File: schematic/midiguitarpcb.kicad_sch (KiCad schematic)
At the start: 35 parts, among them J1 USB_C_Receptacle_USB2.0_16P, J2 AudioJack3_Switch, SW1 SW_Omron_B3FS, U1 AMS1117-3.3, U2 DIN-504D-M5, U3 STM32H743ZITx

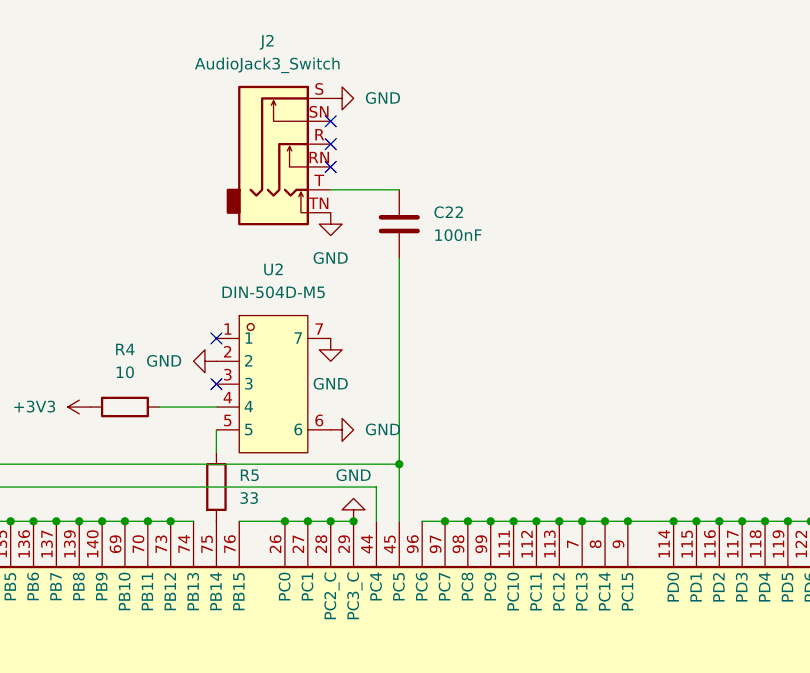
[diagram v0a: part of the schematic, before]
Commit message: chore(wip): about to remove usb code
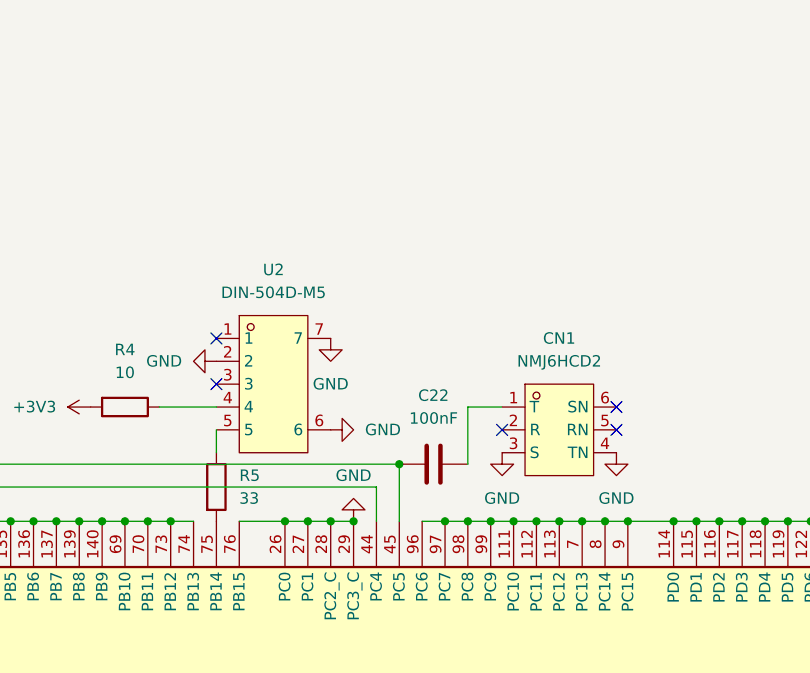
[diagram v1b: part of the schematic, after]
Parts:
- removed J2: AudioJack3_Switch, Connector_Audio:Jack_6.35mm_Neutrik_NMJ6HCD2_Horizontal, symbol Connector_Audio:AudioJack3_Switch
- added CN1: NMJ6HCD2, audio:AUDIO-TH_NMJ6HCD2, symbol audio:NMJ6HCD2
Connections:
- net GND: now also CN1.3 (S), CN1.4 (TN)
- net at C22.1: now also U3.40 (PA4), U3.45 (PC5)
- new net: C22.2, CN1.1 (T)
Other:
- moved on the sheet: C22

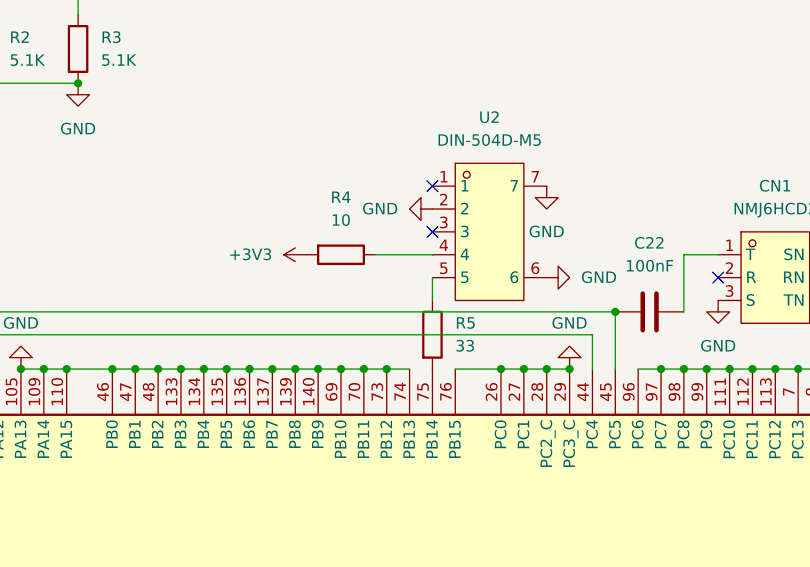
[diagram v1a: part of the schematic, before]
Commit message: fix(pcb): midi resistors swapped
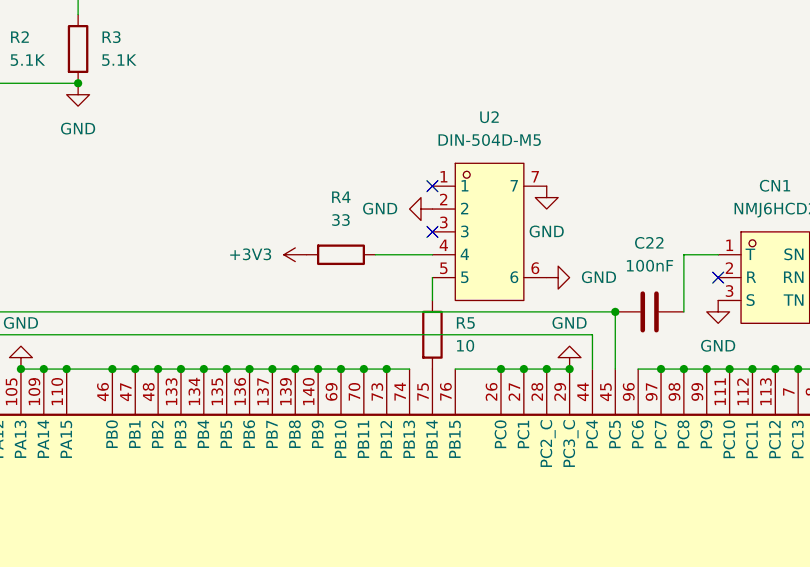
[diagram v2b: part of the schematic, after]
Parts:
- R4: value 10 -> 33
- R5: value 33 -> 10
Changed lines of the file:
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@@
 			)
 		)
-		(property "Value" "10"
+		(property "Value" "33"
 			(at 163.83 71.12 90)
 			(effects
@@
 			)
 		)
-		(property "Value" "33"
+		(property "Value" "10"
 			(at 176.53 85.0899 0)
 			(effects

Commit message: feat(schematic): redo with 2nd opamp
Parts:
- added R5, R6: 100K, Resistor_SMD:R_0402_1005Metric, symbol Device:R
- renumbered C18 to C12, C19 to C17, C20 to C18, C21 to C19, C8 to C20, C17 to C21, C12 to C8, R5 to R7
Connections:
- net +3V3: no longer C20.1, C21.1, U3.32 (VREF+)
- net GND: now also R6.2; no longer U3.1 (PE2), U3.10 (PF0), U3.100 (PA8), U3.101 (PA9), U3.102 (PA10), U3.105 (PA13), U3.109 (PA14), U3.11 (PF1), U3.110 (PA15), U3.111 (PC10), U3.112 (PC11), U3.113 (PC12), U3.114 (PD0), U3.115 (PD1), U3.116 (PD2), U3.117 (PD3), U3.118 (PD4), U3.119 (PD5), U3.12 (PF2), U3.122 (PD6), U3.123 (PD7), U3.124 (PG9), U3.125 (PG10), U3.126 (PG11), U3.127 (PG12), U3.128 (PG13), U3.129 (PG14), U3.13 (PF3), U3.132 (PG15), U3.133 (PB3), U3.134 (PB4), U3.135 (PB5), U3.136 (PB6), U3.137 (PB7), U3.139 (PB8), U3.14 (PF4), U3.140 (PB9), U3.141 (PE0), U3.142 (PE1), U3.15 (PF5), U3.18 (PF6), U3.19 (PF7), U3.2 (PE3), U3.20 (PF8), U3.21 (PF9), U3.22 (PF10), U3.23 (PH0), U3.24 (PH1), U3.26 (PC0), U3.27 (PC1), U3.28 (PC2_C), U3.29 (PC3_C), U3.3 (PE4), U3.34 (PA0), U3.35 (PA1), U3.36 (PA2), U3.37 (PA3), U3.4 (PE5), U3.41 (PA5), U3.42 (PA6), U3.46 (PB0), U3.47 (PB1), U3.48 (PB2), U3.49 (PF11), U3.5 (PE6), U3.50 (PF12), U3.53 (PF13), U3.54 (PF14), U3.55 (PF15), U3.56 (PG0), U3.57 (PG1), U3.58 (PE7), U3.59 (PE8), U3.60 (PE9), U3.63 (PE10), U3.64 (PE11), U3.65 (PE12), U3.66 (PE13), U3.67 (PE14), U3.68 (PE15), U3.69 (PB10), U3.7 (PC13), U3.70 (PB11), U3.73 (PB12), U3.74 (PB13), U3.76 (PB15), U3.77 (PD8), U3.78 (PD9), U3.79 (PD10), U3.8 (PC14), U3.80 (PD11), U3.81 (PD12), U3.82 (PD13), U3.85 (PD14), U3.86 (PD15), U3.87 (PG2), U3.88 (PG3), U3.89 (PG4), U3.9 (PC15), U3.90 (PG5), U3.91 (PG6), U3.92 (PG7), U3.93 (PG8), U3.96 (PC6), U3.97 (PC7), U3.98 (PC8), U3.99 (PC9)
- net at C22.2: now also U3.60 (PE9), R5.1, R6.1; no longer CN1.1 (T)
- new net: C20.1, C21.1, R5.2, U3.32 (VREF+)
- new net: U3.45 (PC5), U3.58 (PE7)
- new net: C22.1, CN1.1 (T)
- now unconnected: U3.40 (PA4)
- no-connect marks 7 -> 113
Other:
- moved on the sheet: C12, C20, C21, C22, C8, CN1
